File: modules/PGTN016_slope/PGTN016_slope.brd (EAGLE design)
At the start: 111.8 x 43.2 mm, 125 parts, among them IC1 LM3900N, IC2 TL074P, IC3 TL074P, Q1 2N3906, Q2 2N3904, Q3 2N3904, Q4 2N3906, Q5 2N3906, Q6 2N3904

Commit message: Added files
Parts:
- added LED+: HEADER/MALE/01, connectors:HEADER/MALE/01
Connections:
- net +12V: now also LED+.1
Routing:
- net +12V: track 218.9 -> 233.6 mm
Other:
- board text added: "2019 Robert Ellis"
- board text added: "PGTN016"
- board text added: "Slope"
- board text removed: "It broke my heart when I learned"
- board text removed: "the moon had been passing"
- board text removed: "the sun's light off as it's own"
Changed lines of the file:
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@@
 <wire x1="115.621" y1="49.52" x2="3.81" y2="49.52" width="0" layer="20"/>
 <wire x1="3.81" y1="49.52" x2="3.81" y2="6.35" width="0" layer="20"/>
-<text x="71.12" y="62.23" size="1.27" layer="25">It broke my heart when I learned</text>
-<text x="71.12" y="59.69" size="1.27" layer="25">the moon had been passing </text>
-<text x="71.12" y="57.15" size="1.27" layer="25">the sun's light off as it's own</text>
+<text x="35.56" y="45.72" size="1.778" layer="25">PGTN016</text>
+<text x="80.01" y="45.72" size="1.778" layer="25">Slope</text>
+<text x="70.866" y="7.112" size="1.27" layer="25">2019 Robert Ellis</text>
 </plain>
 <attributes>
@@
 <element name="U$4" library="mechanical" package="STANDOFF/3.0" value="" x="7.62" y="45.72"/>
 <element name="U$5" library="mechanical" package="PIGATRON-LOGO" value="" x="21.59" y="45.72"/>
+<element name="LED+" library="connectors" package="HEADER/MALE/01" value="HEADER/MALE/01" x="22.86" y="7.62" rot="R90">
+<attribute name="SPICEPREFIX" value="X" x="22.86" y="7.62" size="1.778" layer="27" rot="R90" display="off"/>
+</element>
 </elements>
 <signals>
@@
 <wire x1="15.24" y1="12.7" x2="11.43" y2="16.51" width="0.3048" layer="1"/>
 <wire x1="11.43" y1="16.51" x2="11.43" y2="17.78" width="0.3048" layer="1"/>
+<contactref element="LED+" pad="1"/>
+<wire x1="22.86" y1="13.0175" x2="22.86" y2="7.62" width="0.3048" layer="16"/>
+<wire x1="21.2725" y1="14.605" x2="22.86" y2="13.0175" width="0.3048" layer="16"/>
+<wire x1="16.8275" y1="14.605" x2="21.2725" y2="14.605" width="0.3048" layer="16"/>
+<wire x1="15.24" y1="13.0175" x2="16.8275" y2="14.605" width="0.3048" layer="16"/>
+<wire x1="15.24" y1="12.7" x2="15.24" y2="13.0175" width="0.3048" layer="16"/>
 </signal>
 <signal name="-12V">

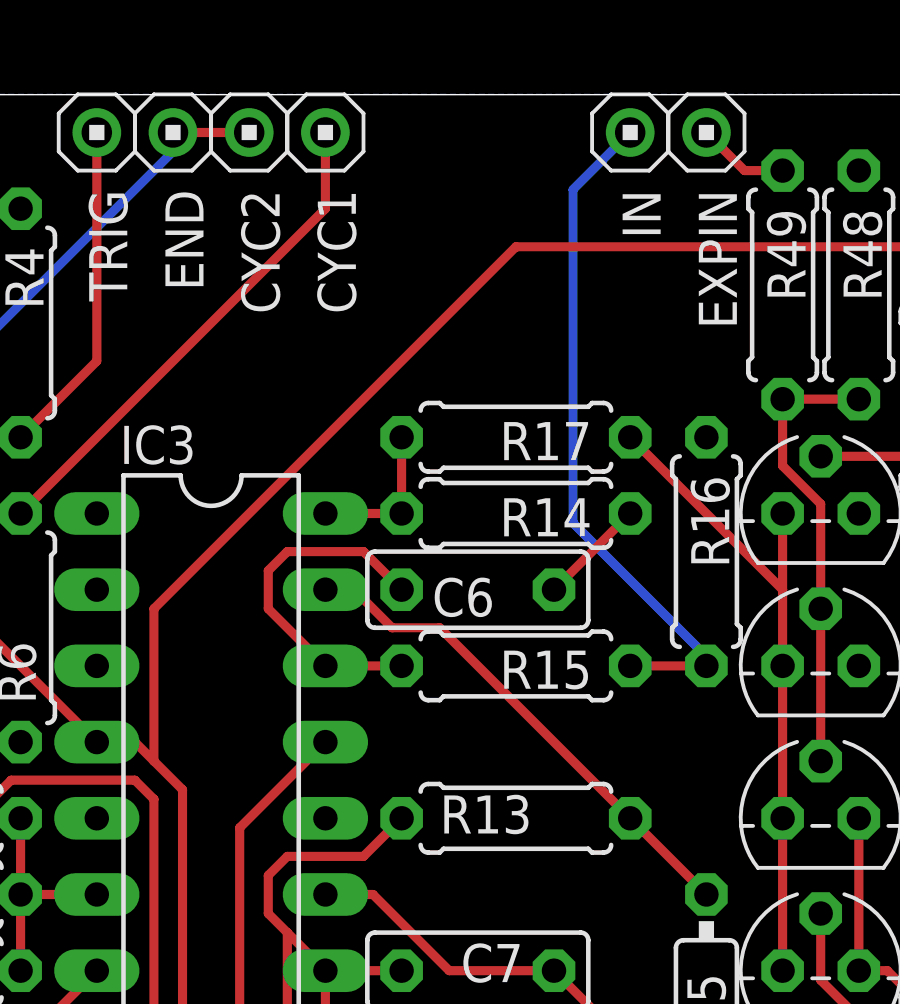
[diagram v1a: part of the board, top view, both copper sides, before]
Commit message: PGTN015 V2 - Fix pins 12 and 13 of IC3 (Op amp inputs) wrong way around.
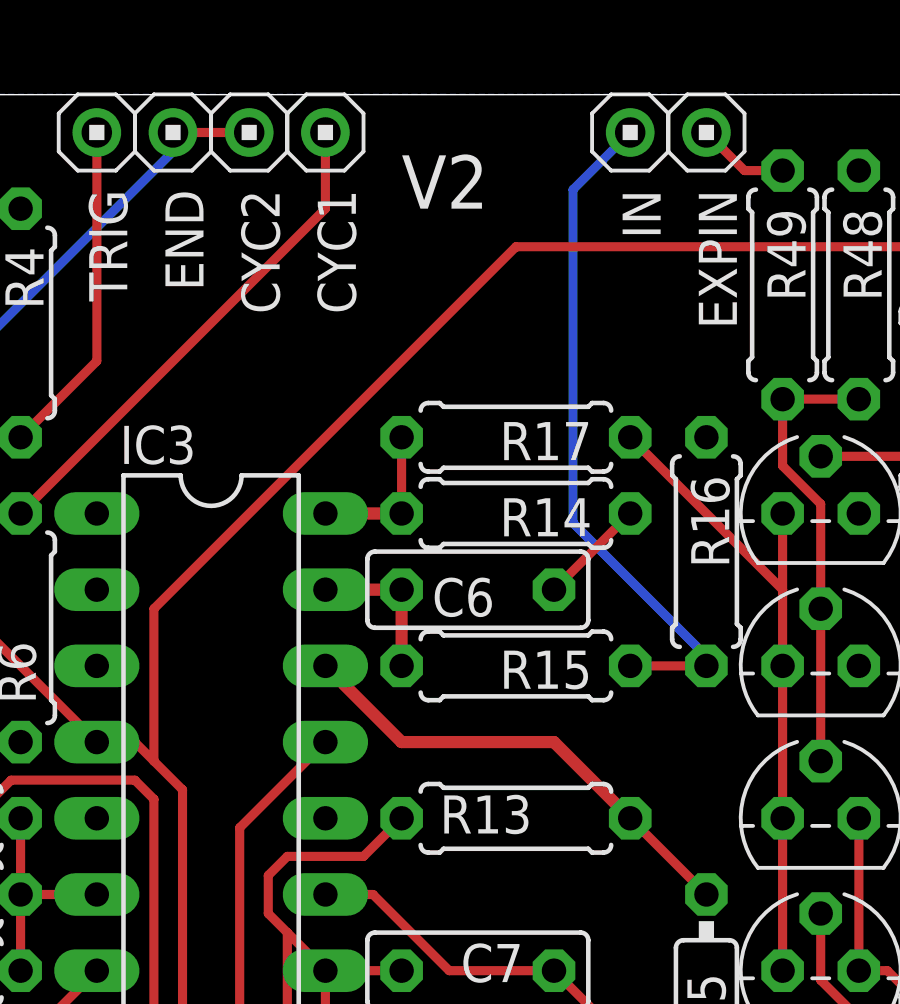
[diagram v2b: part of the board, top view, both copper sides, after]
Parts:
- C12: value (none) -> 47uF
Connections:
- net N$16: now also IC3.12; no longer IC3.13
- net N$20: now also IC3.13; no longer IC3.12
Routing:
- net N$20: track 11.7 -> 5.08 mm
- net N$16: track 16.9 -> 15.9 mm
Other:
- board text added: "V2"
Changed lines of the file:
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@@
 <text x="80.01" y="45.72" size="1.778" layer="25">Slope</text>
 <text x="70.866" y="7.112" size="1.27" layer="25">2019 Robert Ellis</text>
+<text x="60.96" y="45.72" size="1.778" layer="25">V2</text>
 </plain>
 <attributes>
@@
 <element name="D6" library="transistors" package="DO35-7" value="5.6V Zener" x="8.89" y="22.86" rot="R180"/>
 <element name="R55" library="resistors" package="RESISTOR/7.5" value="1M" x="8.89" y="30.48" rot="R180"/>
-<element name="C12" library="capacitors" package="E2,5-6" value="" x="45.72" y="12.7" smashed="yes" rot="R180">
+<element name="C12" library="capacitors" package="E2,5-6" value="47uF" x="45.72" y="12.7" smashed="yes" rot="R180">
 <attribute name="NAME" x="47.244" y="9.525" size="1.27" layer="25" ratio="10" rot="R180"/>
 <attribute name="VALUE" x="43.053" y="15.367" size="1.27" layer="27" ratio="10" rot="R180"/>
@@
 <contactref element="D5" pad="A"/>
 <contactref element="R13" pad="2"/>
-<contactref element="IC3" pad="13"/>
 <wire x1="71.12" y1="22.86" x2="68.58" y2="25.4" width="0.3048" layer="1"/>
-<wire x1="59.3725" y1="33.02" x2="58.42" y2="33.02" width="0.3048" layer="1"/>
-<wire x1="60.6425" y1="31.75" x2="59.3725" y2="33.02" width="0.3048" layer="1"/>
-<wire x1="62.23" y1="31.75" x2="60.6425" y2="31.75" width="0.3048" layer="1"/>
-<wire x1="68.58" y1="25.4" x2="62.23" y2="31.75" width="0.3048" layer="1"/>
+<contactref element="IC3" pad="12"/>
+<wire x1="58.42" y1="30.48" x2="60.96" y2="27.94" width="0.4064" layer="1"/>
+<wire x1="60.96" y1="27.94" x2="66.04" y2="27.94" width="0.4064" layer="1"/>
+<wire x1="66.04" y1="27.94" x2="68.58" y2="25.4" width="0.4064" layer="1"/>
 </signal>
 <signal name="N$18">
 <contactref element="R14" pad="2"/>
 <contactref element="R17" pad="2"/>
+<wire x1="60.96" y1="35.56" x2="60.96" y2="38.1" width="0.3048" layer="1"/>
 <contactref element="IC3" pad="14"/>
-<wire x1="60.96" y1="35.56" x2="58.42" y2="35.56" width="0.3048" layer="1"/>
-<wire x1="60.96" y1="35.56" x2="60.96" y2="38.1" width="0.3048" layer="1"/>
+<wire x1="60.96" y1="35.56" x2="58.42" y2="35.56" width="0.4064" layer="1"/>
 </signal>
 <signal name="N$19">
@@
 <contactref element="C6" pad="1"/>
 <contactref element="R15" pad="2"/>
-<contactref element="IC3" pad="12"/>
-<wire x1="60.96" y1="30.48" x2="58.42" y2="30.48" width="0.3048" layer="1"/>
-<wire x1="59.69" y1="34.29" x2="60.96" y2="33.02" width="0.3048" layer="1"/>
-<wire x1="57.15" y1="34.29" x2="59.69" y2="34.29" width="0.3048" layer="1"/>
-<wire x1="56.515" y1="33.655" x2="57.15" y2="34.29" width="0.3048" layer="1"/>
-<wire x1="56.515" y1="32.385" x2="56.515" y2="33.655" width="0.3048" layer="1"/>
-<wire x1="58.42" y1="30.48" x2="56.515" y2="32.385" width="0.3048" layer="1"/>
+<contactref element="IC3" pad="13"/>
+<wire x1="58.42" y1="33.02" x2="60.96" y2="33.02" width="0.4064" layer="1"/>
+<wire x1="60.96" y1="30.48" x2="60.96" y2="33.02" width="0.4064" layer="1"/>
 </signal>
 <signal name="N$21">
